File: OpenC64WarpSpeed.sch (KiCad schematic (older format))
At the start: 15 parts, among them P1 C64-Exp-Port, SW1 SW_C64_C128, SW2 SW_Push, U1 74LS109, U2 27128

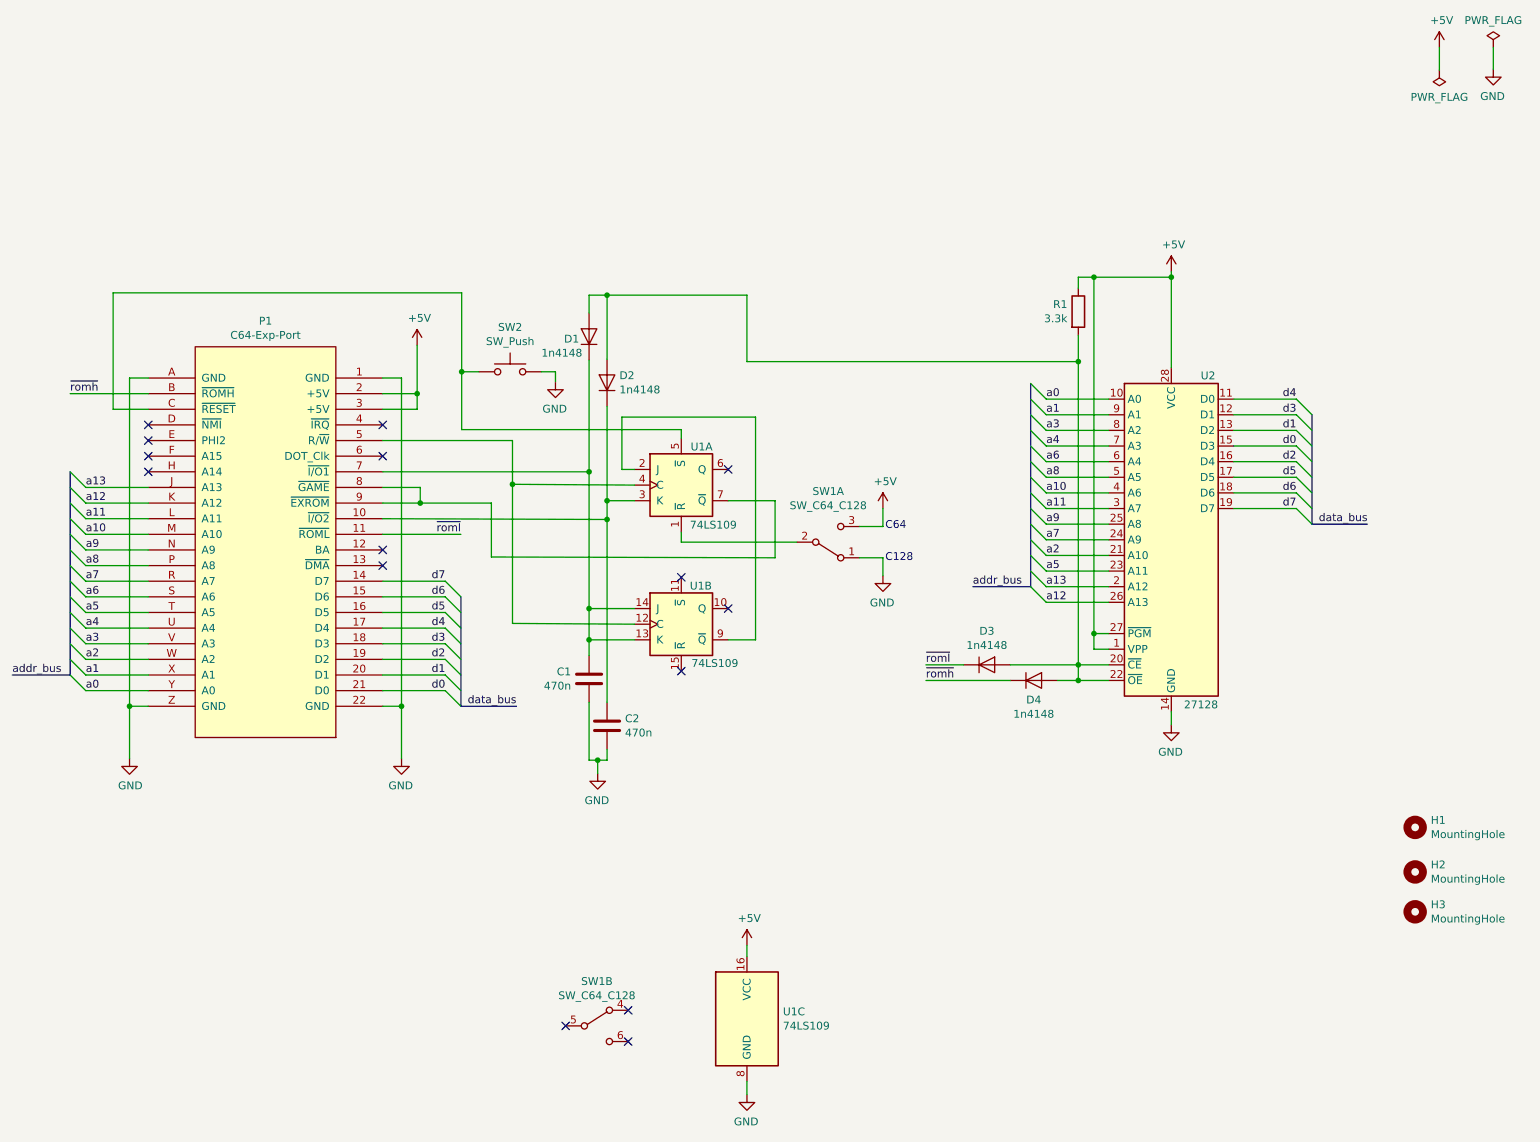
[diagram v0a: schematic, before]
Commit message: Improving the design... - Use ground plane - Add decoupling caps - Avoid scrambling the address and data buses - Switch to 27512
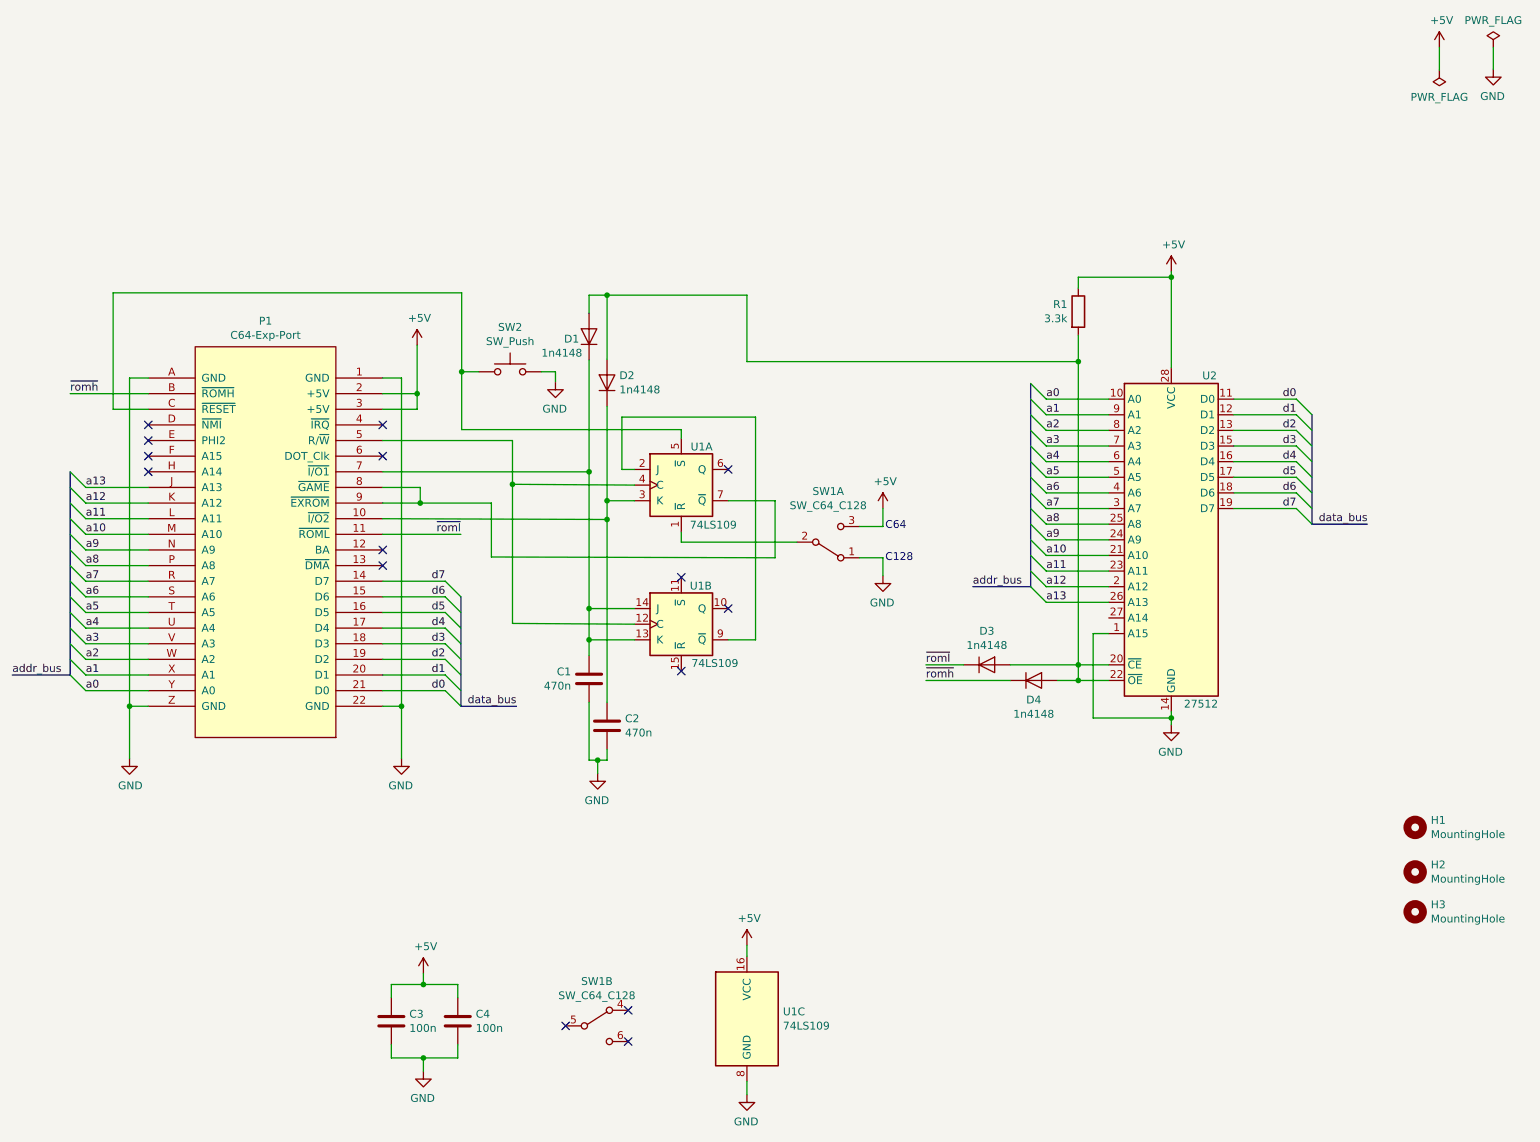
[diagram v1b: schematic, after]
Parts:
- removed U2: 27128, Package_DIP:DIP-28_W15.24mm_Socket_LongPads, symbol Memory_EPROM:27128
- added C3, C4: 100n, Capacitor_THT:C_Disc_D7.5mm_W2.5mm_P5.00mm, symbol Device:C
- added U2: 27512, Package_DIP:DIP-28_W15.24mm, symbol Memory_EPROM:27512
- C1, C2: footprint OpenC64WarpSpeed:C_Disc_D7.5mm_W2.50mm_P7.50mm -> Capacitor_THT:C_Disc_D7.5mm_W2.5mm_P5.00mm
- R1: footprint Resistor_THT:R_Axial_DIN0207_L6.3mm_D2.5mm_P10.16mm_Horizontal -> Resistor_THT:R_Axial_DIN0204_L3.6mm_D1.6mm_P7.62mm_Horizontal
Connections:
- net +5V: now also C3.1, C4.1, U2.28 (VCC)
- net GND: now also C3.2, C4.2, U2.1 (A15), U2.14 (GND)
- net a0: now also U2.10 (A0)
- net a1: now also U2.9 (A1)
- net a10: now also U2.21 (A10)
- net a11: now also U2.23 (A11)
- net a12: now also U2.2 (A12)
- net a13: now also U2.26 (A13)
- net a2: now also U2.8 (A2)
- net a3: now also U2.7 (A3)
- net a4: now also U2.6 (A4)
- net a5: now also U2.5 (A5)
- net a6: now also U2.4 (A6)
- net a7: now also U2.3 (A7)
- net a8: now also U2.25 (A8)
- net a9: now also U2.24 (A9)
- net d0: now also U2.11 (D0)
- net d1: now also U2.12 (D1)
- net d2: now also U2.13 (D2)
- net d3: now also U2.15 (D3)
- net d4: now also U2.16 (D4)
- net d5: now also U2.17 (D5)
- net d6: now also U2.18 (D6)
- net d7: now also U2.19 (D7)
- net at D1.2 (A), D2.2 (A), D3.2 (A)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: now also U2.20 (~CE), U2.22 (~OE)
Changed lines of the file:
@@
 $EndDescr
-$Comp
-L Memory_EPROM:27128 U2
-U 1 1 5F59ABE9
-P 8890 3910
-F 0 "U2" H 9125 4960 50  0000 C CNN
-F 1 "27128" H 9080 2855 50  0000 C CNN
-F 2 "Package_DIP:DIP-28_W15.24mm_Socket_LongPads" H 8890 3910 50  0001 C CNN
-F 3 "http://eeshop.unl.edu/pdf/27128.pdf" H 8890 3910 50  0001 C CNN
-	1    8890 3910
-	1    0    0    -1
-$EndComp
 $Comp
 L 74xx:74LS109 U1
@@
 F 0 "C1" H 5050 4846 50  0000 R CNN
 F 1 "470n" H 5050 4755 50  0000 R CNN
-F 2 "OpenC64WarpSpeed:C_Disc_D7.5mm_W2.50mm_P7.50mm" H 5203 4650 50  0001 C CNN
+F 2 "Capacitor_THT:C_Disc_D7.5mm_W2.5mm_P5.00mm" H 5203 4650 50  0001 C CNN
 F 3 "~" H 5165 4800 50  0001 C CNN
 	1    5165 4800
@@
 F 0 "C2" H 5395 5146 50  0000 L CNN
 F 1 "470n" H 5395 5055 50  0000 L CNN
-F 2 "OpenC64WarpSpeed:C_Disc_D7.5mm_W2.50mm_P7.50mm" H 5318 4950 50  0001 C CNN
+F 2 "Capacitor_THT:C_Disc_D7.5mm_W2.5mm_P5.00mm" H 5318 4950 50  0001 C CNN
 F 3 "~" H 5280 5100 50  0001 C CNN
 	1    5280 5100
@@
 Wire Wire Line
 	9290 3710 9690 3710
-Text Label 9690 3010 2    50   ~ 0
-d4
-Text Label 9690 3110 2    50   ~ 0
-d3
-Text Label 9690 3210 2    50   ~ 0
-d1
-Text Label 9690 3310 2    50   ~ 0
-d0
-Text Label 9690 3410 2    50   ~ 0
-d2
-Text Label 9690 3510 2    50   ~ 0
-d5
-Text Label 9690 3610 2    50   ~ 0
-d6
-Text Label 9690 3710 2    50   ~ 0
-d7
 Entry Wire Line
 	9690 3010 9790 3110
@@
 Entry Wire Line
 	7990 4210 8090 4310
-Text Label 8090 3010 0    50   ~ 0
-a0
-Text Label 8090 3110 0    50   ~ 0
-a1
-Text Label 8090 3210 0    50   ~ 0
-a3
-Text Label 8090 3310 0    50   ~ 0
-a4
-Text Label 8090 3410 0    50   ~ 0
-a6
-Text Label 8090 3510 0    50   ~ 0
-a8
-Text Label 8090 3610 0    50   ~ 0
-a10
-Text Label 8090 3710 0    50   ~ 0
-a11
-Text Label 8090 3810 0    50   ~ 0
-a9
-Text Label 8090 3910 0    50   ~ 0
-a7
-Text Label 8090 4010 0    50   ~ 0
-a2
-Text Label 8090 4110 0    50   ~ 0
-a5
-Text Label 8090 4210 0    50   ~ 0
-a13
-Text Label 8090 4310 0    50   ~ 0
-a12
 Wire Bus Line
 	7990 4210 7620 4210
 Text Label 7620 4210 0    50   ~ 0
 addr_bus
-Wire Wire Line
-	8490 4510 8395 4510
-Wire Wire Line
-	8395 4510 8395 2230
 $Comp
 L power:+5V #PWR0110
@@
 $EndComp
 Wire Wire Line
-	8890 5095 8890 5010
-Wire Wire Line
-	8490 4610 8395 4610
-Wire Wire Line
-	8395 4610 8395 4510
-Connection ~ 8395 4510
+	8890 5095 8890 5050
 Wire Wire Line
 	8490 4710 8295 4710
 Wire Wire Line
 	8490 4810 8295 4810
-Wire Wire Line
-	8395 2230 8890 2230
 Connection ~ 8890 2230
 Wire Wire Line
@@
 F 0 "R1" H 8225 2496 50  0000 R CNN
 F 1 "3.3k" H 8225 2405 50  0000 R CNN
-F 2 "Resistor_THT:R_Axial_DIN0207_L6.3mm_D2.5mm_P10.16mm_Horizontal" V 8225 2450 50  0001 C CNN
+F 2 "Resistor_THT:R_Axial_DIN0204_L3.6mm_D1.6mm_P7.62mm_Horizontal" V 8225 2450 50  0001 C CNN
 F 3 "~" H 8295 2450 50  0001 C CNN
 	1    8295 2450
@@
 Wire Wire Line
 	8295 2300 8295 2230
-Wire Wire Line
-	8295 2230 8395 2230
-Connection ~ 8395 2230
 Wire Wire Line
 	6175 2770 8295 2770
@@
 NoConn ~ 5415 7120
 NoConn ~ 5015 7020
+Text Label 8090 3010 0    50   ~ 0
+a0
+Text Label 8090 3110 0    50   ~ 0
+a1
+Text Label 8090 3210 0    50   ~ 0
+a2
+Text Label 8090 3310 0    50   ~ 0
+a3
+Text Label 8090 3410 0    50   ~ 0
+a4
+Text Label 8090 3510 0    50   ~ 0
+a5
+Text Label 8090 3610 0    50   ~ 0
+a6
+Text Label 8090 3710 0    50   ~ 0
+a7
+Text Label 8090 3810 0    50   ~ 0
+a8
+Text Label 8090 3910 0    50   ~ 0
+a9
+Text Label 8090 4010 0    50   ~ 0
+a10
+Text Label 8090 4110 0    50   ~ 0
+a11
+Text Label 8090 4210 0    50   ~ 0
+a12
+Text Label 8090 4310 0    50   ~ 0
+a13
+Text Label 9690 3010 2    50   ~ 0
+d0
+Text Label 9690 3110 2    50   ~ 0
+d1
+Text Label 9690 3210 2    50   ~ 0
+d2
+Text Label 9690 3310 2    50   ~ 0
+d3
+Text Label 9690 3410 2    50   ~ 0
+d4
+Text Label 9690 3510 2    50   ~ 0
+d5
+Text Label 9690 3610 2    50   ~ 0
+d6
+Text Label 9690 3710 2    50   ~ 0
+d7
+$Comp
+L Device:C C3
+U 1 1 5F7F7C81
+P 3900 6990
+F 0 "C3" H 4015 7036 50  0000 L CNN
+F 1 "100n" H 4015 6945 50  0000 L CNN
+F 2 "Capacitor_THT:C_Disc_D7.5mm_W2.5mm_P5.00mm" H 3938 6840 50  0001 C CNN
+F 3 "~" H 3900 6990 50  0001 C CNN
+	1    3900 6990
+	1    0    0    -1
+$EndComp
+$Comp
+L Device:C C4
+U 1 1 5F7F85EA
+P 4325 6990
+F 0 "C4" H 4440 7036 50  0000 L CNN
+F 1 "100n" H 4440 6945 50  0000 L CNN
+F 2 "Capacitor_THT:C_Disc_D7.5mm_W2.5mm_P5.00mm" H 4363 6840 50  0001 C CNN
+F 3 "~" H 4325 6990 50  0001 C CNN
+	1    4325 6990
+	1    0    0    -1
+$EndComp
+Wire Wire Line
+	3900 6840 3900 6755
+Wire Wire Line
+	3900 6755 4105 6755
+Wire Wire Line
+	4325 6755 4325 6840
+Wire Wire Line
+	3900 7140 3900 7225
+Wire Wire Line
+	3900 7225 4105 7225
+Wire Wire Line
+	4325 7225 4325 7140
+$Comp
+L power:GND #PWR02
+U 1 1 5F803318
+P 4105 7310
+F 0 "#PWR02" H 4105 7060 50  0001 C CNN
+F 1 "GND" H 4110 7137 50  0000 C CNN
+F 2 "" H 4105 7310 50  0001 C CNN
+F 3 "" H 4105 7310 50  0001 C CNN
+	1    4105 7310
+	-1   0    0    -1
+$EndComp
+Wire Wire Line
+	4105 7310 4105 7225
+Connection ~ 4105 7225
+Wire Wire Line
+	4105 7225 4325 7225
+$Comp
+L power:+5V #PWR01
+U 1 1 5F8090BC
+P 4105 6685
+F 0 "#PWR01" H 4105 6535 50  0001 C CNN
+F 1 "+5V" H 4120 6858 50  0000 C CNN
+F 2 "" H 4105 6685 50  0001 C CNN
+F 3 "" H 4105 6685 50  0001 C CNN
+	1    4105 6685
+	1    0    0    -1
+$EndComp
+Wire Wire Line
+	4105 6685 4105 6755
+Connection ~ 4105 6755
+Wire Wire Line
+	4105 6755 4325 6755
+$Comp
+L Memory_EPROM:27512 U2
+U 1 1 5F80FF67
+P 8890 3910
+F 0 "U2" H 9135 4960 50  0000 C CNN
+F 1 "27512" H 9080 2860 50  0000 C CNN
+F 2 "Package_DIP:DIP-28_W15.24mm" H 8890 3910 50  0001 C CNN
+F 3 "http://pdf.datasheetcatalog.com/datasheets/120/227190_DS.pdf" H 8890 3910 50  0001 C CNN
+	1    8890 3910
+	1    0    0    -1
+$EndComp
+Wire Wire Line
+	8295 2230 8890 2230
+Wire Wire Line
+	8490 4510 8390 4510
+Wire Wire Line
+	8390 4510 8390 5050
+Wire Wire Line
+	8390 5050 8890 5050
 Wire Bus Line
 	4345 4275 4345 4975
@@
 Wire Bus Line
 	7990 2910 7990 4210
+Connection ~ 8890 5050
+Wire Wire Line
+	8890 5050 8890 5010
 $EndSCHEMATC

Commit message: Almost there
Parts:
- U2: footprint Package_DIP:DIP-28_W15.24mm -> Package_DIP:DIP-28_W15.24mm_Socket_LongPads
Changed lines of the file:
@@
 F 0 "U2" H 9135 4960 50  0000 C CNN
 F 1 "27512" H 9080 2860 50  0000 C CNN
-F 2 "Package_DIP:DIP-28_W15.24mm" H 8890 3910 50  0001 C CNN
+F 2 "Package_DIP:DIP-28_W15.24mm_Socket_LongPads" H 8890 3910 50  0001 C CNN
 F 3 "http://pdf.datasheetcatalog.com/datasheets/120/227190_DS.pdf" H 8890 3910 50  0001 C CNN
 	1    8890 3910

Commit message: I guess we're good, just need to work on the ground plane yet
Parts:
- added SW3: SW_ROM, OpenC64WarpSpeed:SW_DPDT, symbol Switch:SW_DPDT_x2
- SW2: value SW_Push -> SW_RESET
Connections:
- net +5V: now also SW3.1 (A)
- net GND: now also SW3.3 (C)
- net at U2.27 (A14): now also SW3.2 (B)
- no-connect marks 15 -> 18
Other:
- moved on the sheet: C3, C4, R1, SW1B
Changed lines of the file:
@@
 P 4660 2835
 F 0 "SW2" H 4660 3120 50  0000 C CNN
-F 1 "SW_Push" H 4660 3029 50  0000 C CNN
+F 1 "SW_RESET" H 4660 3029 50  0000 C CNN
 F 2 "Button_Switch_THT:SW_PUSH_6mm" H 4660 3035 50  0001 C CNN
 F 3 "~" H 4660 3035 50  0001 C CNN
@@
 L power:+5V #PWR0110
 U 1 1 5F62B802
-P 8890 2195
-F 0 "#PWR0110" H 8890 2045 50  0001 C CNN
-F 1 "+5V" H 8905 2368 50  0000 C CNN
-F 2 "" H 8890 2195 50  0001 C CNN
-F 3 "" H 8890 2195 50  0001 C CNN
-	1    8890 2195
-	1    0    0    -1
-$EndComp
-Wire Wire Line
-	8890 2195 8890 2230
+P 8890 2250
+F 0 "#PWR0110" H 8890 2100 50  0001 C CNN
+F 1 "+5V" H 8905 2423 50  0000 C CNN
+F 2 "" H 8890 2250 50  0001 C CNN
+F 3 "" H 8890 2250 50  0001 C CNN
+	1    8890 2250
+	1    0    0    -1
+$EndComp
+Wire Wire Line
+	8890 2250 8890 2285
 $Comp
 L power:GND #PWR0111
@@
 Wire Wire Line
 	8490 4810 8295 4810
-Connection ~ 8890 2230
-Wire Wire Line
-	8890 2230 8890 2810
+Connection ~ 8890 2285
+Wire Wire Line
+	8890 2285 8890 2810
 $Comp
 L Device:D D3
@@
 L Device:R R1
 U 1 1 5F66CE22
-P 8295 2450
-F 0 "R1" H 8225 2496 50  0000 R CNN
-F 1 "3.3k" H 8225 2405 50  0000 R CNN
-F 2 "Resistor_THT:R_Axial_DIN0204_L3.6mm_D1.6mm_P7.62mm_Horizontal" V 8225 2450 50  0001 C CNN
-F 3 "~" H 8295 2450 50  0001 C CNN
-	1    8295 2450
-	1    0    0    -1
-$EndComp
-Wire Wire Line
-	8295 2300 8295 2230
+P 8295 2505
+F 0 "R1" H 8225 2551 50  0000 R CNN
+F 1 "3.3k" H 8225 2460 50  0000 R CNN
+F 2 "Resistor_THT:R_Axial_DIN0204_L3.6mm_D1.6mm_P7.62mm_Horizontal" V 8225 2505 50  0001 C CNN
+F 3 "~" H 8295 2505 50  0001 C CNN
+	1    8295 2505
+	1    0    0    -1
+$EndComp
+Wire Wire Line
+	8295 2355 8295 2285
 Wire Wire Line
 	6175 2770 8295 2770
 Connection ~ 8295 2770
 Wire Wire Line
-	8295 2770 8295 2600
+	8295 2770 8295 2655
 $Comp
 L power:+5V #PWR0112
@@
 L Switch:SW_DPDT_x2 SW1
 U 2 1 5F6F8CDC
-P 5215 7020
-F 0 "SW1" H 5215 7305 50  0000 C CNN
-F 1 "SW_C64_C128" H 5215 7214 50  0000 C CNN
-F 2 "OpenC64WarpSpeed:SW_DPDT" H 5215 7020 50  0001 C CNN
-F 3 "~" H 5215 7020 50  0001 C CNN
-	2    5215 7020
-	1    0    0    -1
-$EndComp
-NoConn ~ 5415 6920
-NoConn ~ 5415 7120
-NoConn ~ 5015 7020
+P 5260 7020
+F 0 "SW1" H 5260 7305 50  0000 C CNN
+F 1 "SW_C64_C128" H 5260 7214 50  0000 C CNN
+F 2 "OpenC64WarpSpeed:SW_DPDT" H 5260 7020 50  0001 C CNN
+F 3 "~" H 5260 7020 50  0001 C CNN
+	2    5260 7020
+	1    0    0    -1
+$EndComp
+NoConn ~ 5460 6920
+NoConn ~ 5460 7120
+NoConn ~ 5060 7020
 Text Label 8090 3010 0    50   ~ 0
 a0
@@
 L Device:C C3
 U 1 1 5F7F7C81
-P 3900 6990
-F 0 "C3" H 4015 7036 50  0000 L CNN
-F 1 "100n" H 4015 6945 50  0000 L CNN
-F 2 "Capacitor_THT:C_Disc_D7.5mm_W2.5mm_P5.00mm" H 3938 6840 50  0001 C CNN
-F 3 "~" H 3900 6990 50  0001 C CNN
-	1    3900 6990
+P 3280 6975
+F 0 "C3" H 3395 7021 50  0000 L CNN
+F 1 "100n" H 3395 6930 50  0000 L CNN
+F 2 "Capacitor_THT:C_Disc_D7.5mm_W2.5mm_P5.00mm" H 3318 6825 50  0001 C CNN
+F 3 "~" H 3280 6975 50  0001 C CNN
+	1    3280 6975
 	1    0    0    -1
 $EndComp
@@
 L Device:C C4
 U 1 1 5F7F85EA
-P 4325 6990
-F 0 "C4" H 4440 7036 50  0000 L CNN
-F 1 "100n" H 4440 6945 50  0000 L CNN
-F 2 "Capacitor_THT:C_Disc_D7.5mm_W2.5mm_P5.00mm" H 4363 6840 50  0001 C CNN
-F 3 "~" H 4325 6990 50  0001 C CNN
-	1    4325 6990
-	1    0    0    -1
-$EndComp
-Wire Wire Line
-	3900 6840 3900 6755
-Wire Wire Line
-	3900 6755 4105 6755
-Wire Wire Line
-	4325 6755 4325 6840
-Wire Wire Line
-	3900 7140 3900 7225
-Wire Wire Line
-	3900 7225 4105 7225
-Wire Wire Line
-	4325 7225 4325 7140
+P 3705 6975
+F 0 "C4" H 3820 7021 50  0000 L CNN
+F 1 "100n" H 3820 6930 50  0000 L CNN
+F 2 "Capacitor_THT:C_Disc_D7.5mm_W2.5mm_P5.00mm" H 3743 6825 50  0001 C CNN
+F 3 "~" H 3705 6975 50  0001 C CNN
+	1    3705 6975
+	1    0    0    -1
+$EndComp
+Wire Wire Line
+	3280 6825 3280 6740
+Wire Wire Line
+	3280 6740 3485 6740
+Wire Wire Line
+	3705 6740 3705 6825
+Wire Wire Line
+	3280 7125 3280 7210
+Wire Wire Line
+	3280 7210 3485 7210
+Wire Wire Line
+	3705 7210 3705 7125
 $Comp
 L power:GND #PWR02
 U 1 1 5F803318
-P 4105 7310
-F 0 "#PWR02" H 4105 7060 50  0001 C CNN
-F 1 "GND" H 4110 7137 50  0000 C CNN
-F 2 "" H 4105 7310 50  0001 C CNN
-F 3 "" H 4105 7310 50  0001 C CNN
-	1    4105 7310
-	-1   0    0    -1
-$EndComp
-Wire Wire Line
-	4105 7310 4105 7225
-Connection ~ 4105 7225
-Wire Wire Line
-	4105 7225 4325 7225
+P 3485 7295
+F 0 "#PWR02" H 3485 7045 50  0001 C CNN
+F 1 "GND" H 3490 7122 50  0000 C CNN
+F 2 "" H 3485 7295 50  0001 C CNN
+F 3 "" H 3485 7295 50  0001 C CNN
+	1    3485 7295
+	-1   0    0    -1
+$EndComp
+Wire Wire Line
+	3485 7295 3485 7210
+Connection ~ 3485 7210
+Wire Wire Line
+	3485 7210 3705 7210
 $Comp
 L power:+5V #PWR01
 U 1 1 5F8090BC
-P 4105 6685
-F 0 "#PWR01" H 4105 6535 50  0001 C CNN
-F 1 "+5V" H 4120 6858 50  0000 C CNN
-F 2 "" H 4105 6685 50  0001 C CNN
-F 3 "" H 4105 6685 50  0001 C CNN
-	1    4105 6685
-	1    0    0    -1
-$EndComp
-Wire Wire Line
-	4105 6685 4105 6755
-Connection ~ 4105 6755
-Wire Wire Line
-	4105 6755 4325 6755
+P 3485 6670
+F 0 "#PWR01" H 3485 6520 50  0001 C CNN
+F 1 "+5V" H 3500 6843 50  0000 C CNN
+F 2 "" H 3485 6670 50  0001 C CNN
+F 3 "" H 3485 6670 50  0001 C CNN
+	1    3485 6670
+	1    0    0    -1
+$EndComp
+Wire Wire Line
+	3485 6670 3485 6740
+Connection ~ 3485 6740
+Wire Wire Line
+	3485 6740 3705 6740
 $Comp
 L Memory_EPROM:27512 U2
@@
 $EndComp
 Wire Wire Line
-	8295 2230 8890 2230
+	8295 2285 8890 2285
 Wire Wire Line
 	8490 4510 8390 4510
@@
 Wire Wire Line
 	8390 5050 8890 5050
+Connection ~ 8890 5050
+Wire Wire Line
+	8890 5050 8890 5010
+$Comp
+L Switch:SW_DPDT_x2 SW3
+U 1 1 5F89C548
+P 6695 4410
+F 0 "SW3" H 6695 4085 50  0000 C CNN
+F 1 "SW_ROM" H 6695 4176 50  0000 C CNN
+F 2 "OpenC64WarpSpeed:SW_DPDT" H 6695 4410 50  0001 C CNN
+F 3 "~" H 6695 4410 50  0001 C CNN
+	1    6695 4410
+	-1   0    0    -1
+$EndComp
+Wire Wire Line
+	8490 4410 6895 4410
+Wire Wire Line
+	6495 4510 6345 4510
+Wire Wire Line
+	6345 4510 6345 4625
+$Comp
+L power:GND #PWR0114
+U 1 1 5F8A4D13
+P 6345 4625
+F 0 "#PWR0114" H 6345 4375 50  0001 C CNN
+F 1 "GND" H 6350 4452 50  0000 C CNN
+F 2 "" H 6345 4625 50  0001 C CNN
+F 3 "" H 6345 4625 50  0001 C CNN
+	1    6345 4625
+	1    0    0    -1
+$EndComp
+Wire Wire Line
+	6495 4310 6345 4310
+Wire Wire Line
+	6345 4310 6345 4265
+$Comp
+L power:+5V #PWR0115
+U 1 1 5F8AB034
+P 6345 4265
+F 0 "#PWR0115" H 6345 4115 50  0001 C CNN
+F 1 "+5V" H 6360 4438 50  0000 C CNN
+F 2 "" H 6345 4265 50  0001 C CNN
+F 3 "" H 6345 4265 50  0001 C CNN
+	1    6345 4265
+	-1   0    0    -1
+$EndComp
+$Comp
+L Switch:SW_DPDT_x2 SW3
+U 2 1 5F8C4CFE
+P 4470 7020
+F 0 "SW3" H 4470 7305 50  0000 C CNN
+F 1 "SW_ROM" H 4470 7214 50  0000 C CNN
+F 2 "OpenC64WarpSpeed:SW_DPDT" H 4470 7020 50  0001 C CNN
+F 3 "~" H 4470 7020 50  0001 C CNN
+	2    4470 7020
+	1    0    0    -1
+$EndComp
+NoConn ~ 4670 6920
+NoConn ~ 4670 7120
+NoConn ~ 4270 7020
 Wire Bus Line
 	4345 4275 4345 4975
@@
 Wire Bus Line
 	7990 2910 7990 4210
-Connection ~ 8890 5050
-Wire Wire Line
-	8890 5050 8890 5010
 $EndSCHEMATC
